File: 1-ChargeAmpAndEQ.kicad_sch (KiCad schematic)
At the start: 53 parts, among them J101 6.3mm stereo, J102 6.3mm stereo, U101 OPA145, U102 OPA145

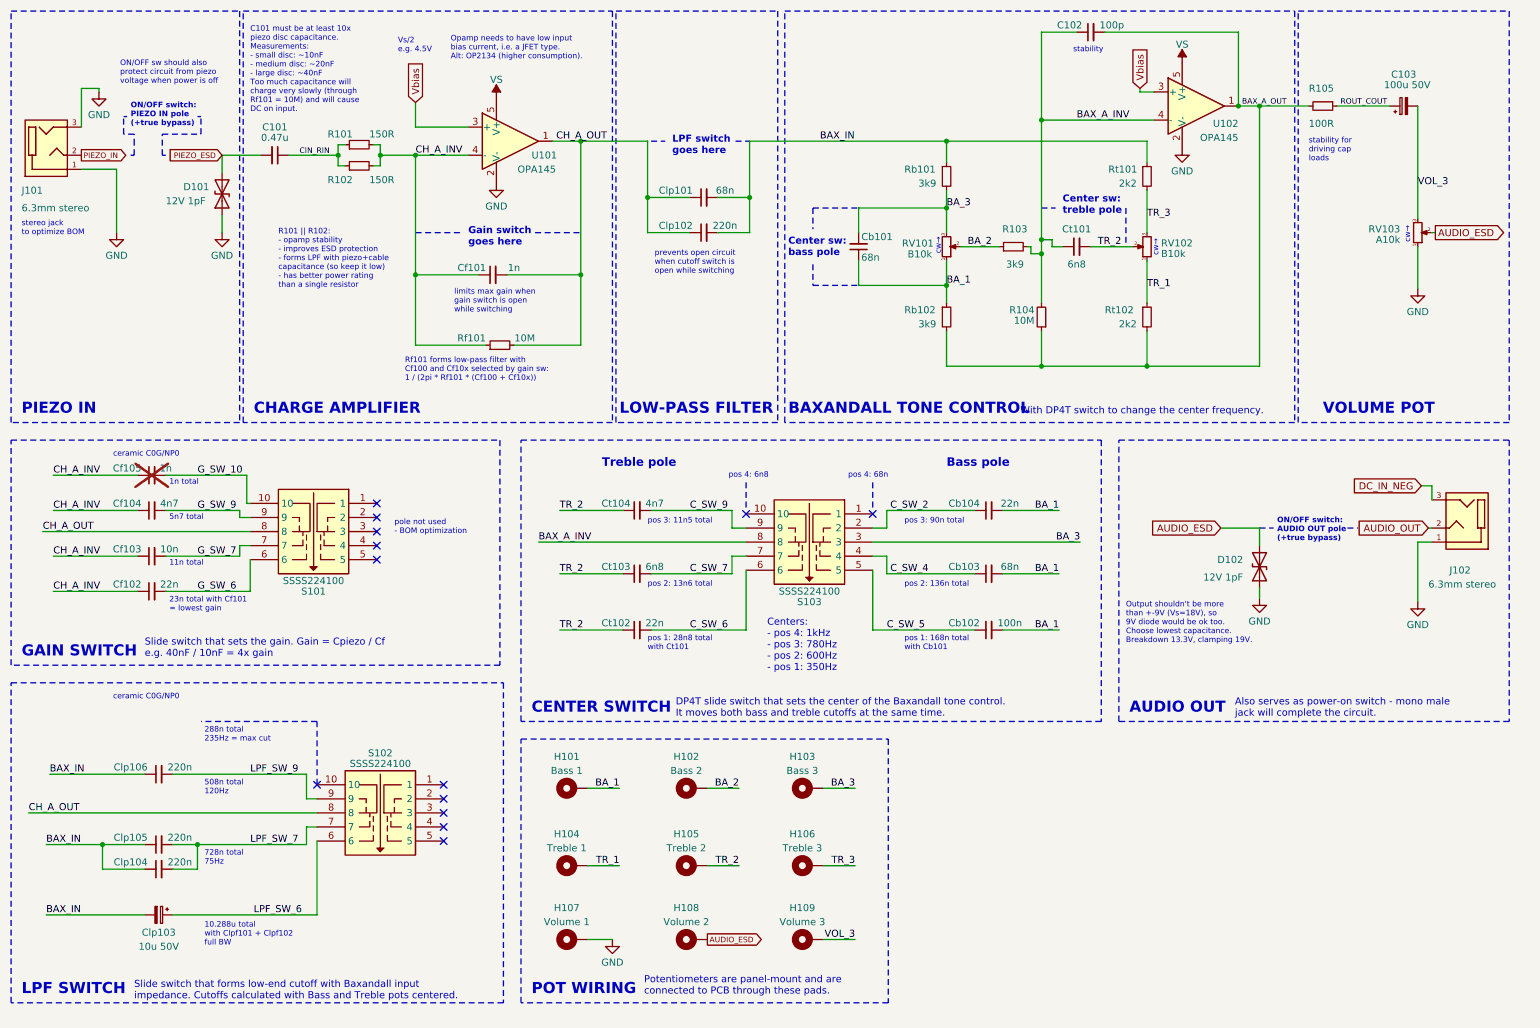
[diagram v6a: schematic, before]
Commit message: schematics: heavy BOM optimization, many small changes, filling missing fields, improving symbols and everything
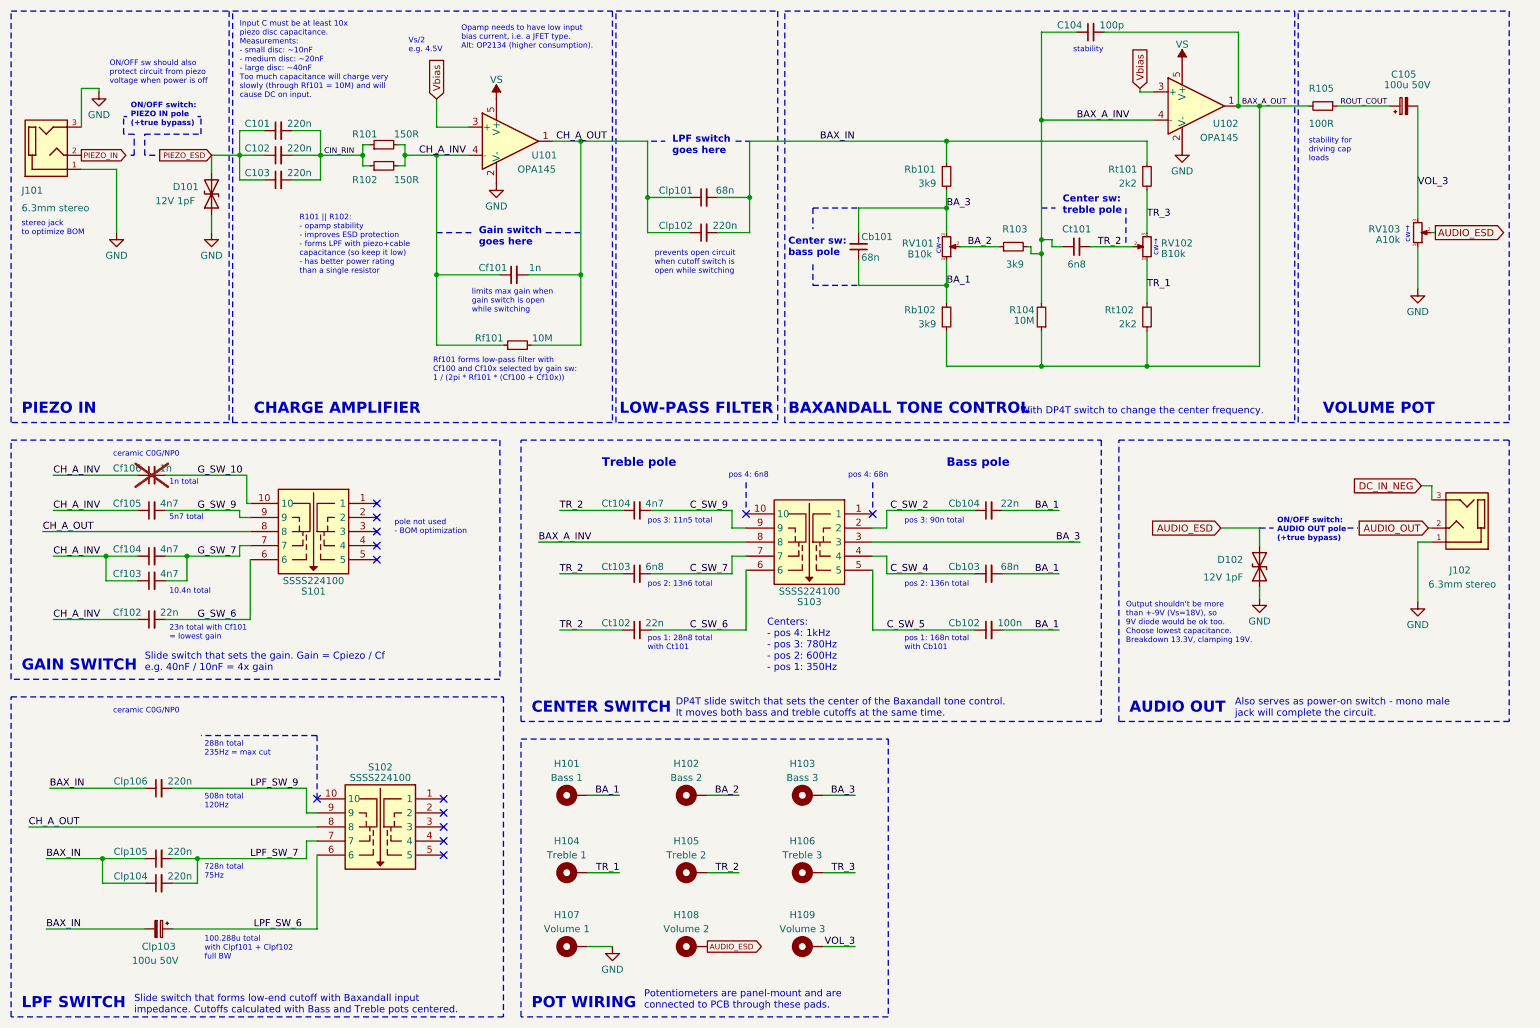
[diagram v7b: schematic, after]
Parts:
- added C102, C103: 220n, library:GRM31C5C1H224JE02L, symbol Device:C_Small
- added Cf104: 4n7, library:GRM1885C1H472JA01D, symbol Device:C_Small
- C101: value 0.47u -> 220n; footprint library:GRM31C5C1E474JE01L -> library:GRM31C5C1H224JE02L; LCSC Part # C6049896 -> C464977; Mfr Part # GRM31C5C1E474JE01L -> GRM31C5C1H224JE02L; Mouser Part # 81-GRM31C5C1E474JE1L -> 81-GRM31C5C1H224JE2L; Source Mouser -> LCSC; TME Part # GRM31C5C1E474JE01L -> (none)
- C104: renamed from C102; footprint library:GRM1885C1H101JA01D -> library:cap_CL10C101JB8NNNC; LCSC Part # C71664 -> C14858; Mfr Murata -> Samsung; Mfr Part # GRM1885C1H101JA01D -> CL10C101JB8NNNC; Mouser Part # 81-GRM39C101J50 -> 187-CL10C101JB8NNNC; Source (none) -> LCSC
- C105: renamed from C103; Source (none) -> LCSC
- Cb101, Cb102, Cb103, Cf101, Clp101, Clp102, Clp104, Clp105, Clp106, Ct101, Ct103, Ct104, D101, D102, R101, R102, R103, R105, Rb101, Rb102, Rt101, Rt102: Source (none) -> LCSC
- Cb104, Cf102, Ct102: footprint library:CGA4J2C0G1H223J125AA -> library:GRM21B5C1H223JA01L; LCSC Part # C415303 -> C77069; Mfr TDK -> Murata; Mfr Part # CGA4J2C0G1H223J125AA -> GRM21B5C1H223JA01L; Mouser Part # 810-CGA4J2C0G1H223J -> 81-GRM215C1H223JA01L; Source (none) -> LCSC
- Cf103: value 10n -> 4n7; footprint library:GRM1885C1H103JA01D -> library:GRM1885C1H472JA01D; LCSC Part # C85973 -> C85980; Mfr Part # GRM1885C1H103JA01D -> GRM1885C1H472JA01D; Mouser Part # 81-GRM1885C1H103JA1D -> 81-GRM1885C1H472JA1D; Source (none) -> LCSC
- Cf105: renamed from Cf104; Source (none) -> LCSC
- Cf106: renamed from Cf105; Source (none) -> LCSC
- Clp103: value 10u 50V -> 100u 50V; footprint library:EEEFK1H100UR -> library:EEEFTH101XAP; LCSC Part # C178547 -> C165974; Mfr Part # EEEFK1H100UR -> EEEFTH101XAP; Mouser Part # 667-EEE-FK1H100UR -> 667-EEE-FTH101XAP; Purpose LPF - sets low-pass cutoff frequency -> AC coupling / DC blocking; Source (none) -> LCSC
- H101, H102, H103, H104, H105, H106, H107, H108, H109: Source (none) -> -
- J101, J102, R104, Rf101, S101, S102, S103, U101, U102: Source (none) -> Mouser
- RV101, RV102, RV103: Source (none) -> TME
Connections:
- net CH_A_INV: now also Cf104.1
- net CIN_RIN: now also C101.2, C102.2, C103.2; no longer C101.1
- net G_SW_7: now also Cf104.2
- net PIEZO_ESD: now also C101.1, C102.1, C103.1; no longer C101.2
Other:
- note added: "10.4n total"
- note added: "100.288u total with Clpf101 + Clpf102 full BW"
- note added: "Input C must be at least 10x piezo disc capacitance. Measurements: - small disc: ~10nF - medium disc: ~20nF - large disc: ~40nF Too much capacitance will charge very slowly (through Rf101 = 10M) and will cause DC on input."
- note removed: "10.288u total with Clpf101 + Clpf102 full BW"
- note removed: "11n total"
- note removed: "C101 must be at least 10x piezo disc capacitance. Measurements: - small disc: ~10nF - medium disc: ~20nF - large disc: ~40nF Too much capacitance will charge very slowly (through Rf101 = 10M) and will cause DC on input."
- moved on the sheet: Cf101, Cf102, Clp104, Clp105, Clp106, D101, H101, H102, H103, H104, H105, H106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

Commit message: aligning schematics to grid, swapping switches as they are on the bottom side now; rough placement of BI section on board
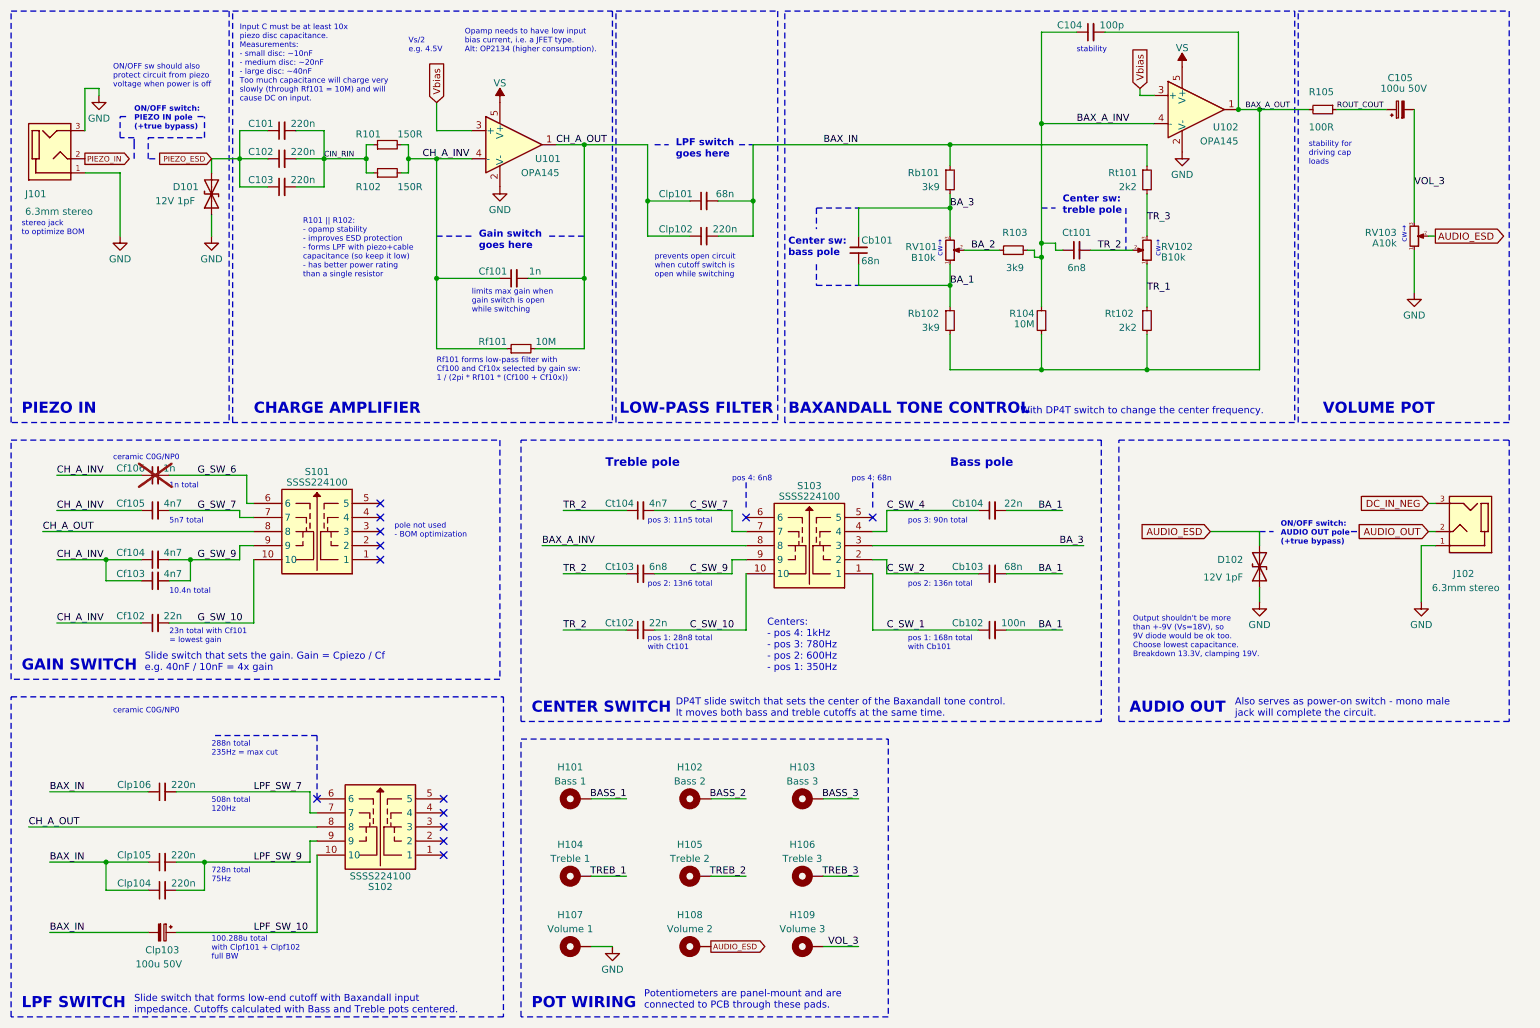
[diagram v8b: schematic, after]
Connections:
- net BA_1: no longer H101.1
- net BA_2: no longer H102.1
- net BA_3: no longer H103.1
- net C_SW_2: now also Cb103.1; no longer Cb104.1
- net C_SW_4: now also Cb104.1; no longer Cb103.1
- net C_SW_7: now also Ct104.2; no longer Ct103.2
- net C_SW_9: now also Ct103.2; no longer Ct104.2
- net G_SW_10: now also Cf102.2; no longer Cf106.2
- net G_SW_6: now also Cf106.2; no longer Cf102.2
- net G_SW_7: now also Cf105.2; no longer Cf103.2, Cf104.2
- net G_SW_9: now also Cf103.2, Cf104.2; no longer Cf105.2
- net LPF_SW_7: now also Clp106.2; no longer Clp104.2, Clp105.2
- net LPF_SW_9: now also Clp104.2, Clp105.2; no longer Clp106.2
- net TR_1: no longer H104.1
- net TR_2: no longer H105.1
- net TR_3: no longer H106.1
- net C_SW_1: now reaches S103.1
- net C_SW_1: now also Cb102.1
- net C_SW_10: now reaches S103.10
- net C_SW_10: now also Ct102.2
- net LPF_SW_10: now reaches S102.10
- net LPF_SW_10: now also Clp103.1
- net C_SW_5: no longer names the net of S103.5
- net C_SW_5: no longer Cb102.1
- net C_SW_6: no longer names the net of S103.6
- net C_SW_6: no longer Ct102.2
- net LPF_SW_6: no longer names the net of S102.6
- net LPF_SW_6: no longer Clp103.1
- new net BASS_1: H101.1
- new net BASS_2: H102.1
- new net BASS_3: H103.1
- new net TREB_1: H104.1
- new net TREB_2: H105.1
- new net TREB_3: H106.1
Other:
- moved on the sheet: C101, C102, C103, C105, Cb101, Cb102, Cb103, Cb104, Cf101, Cf102, Cf103, Cf104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
